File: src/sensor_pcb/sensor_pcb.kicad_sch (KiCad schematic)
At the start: 11 parts, among them Q1 NPN BJT 40V 200mA, U1 SHT45-AD1B, U2 16-bit ADC

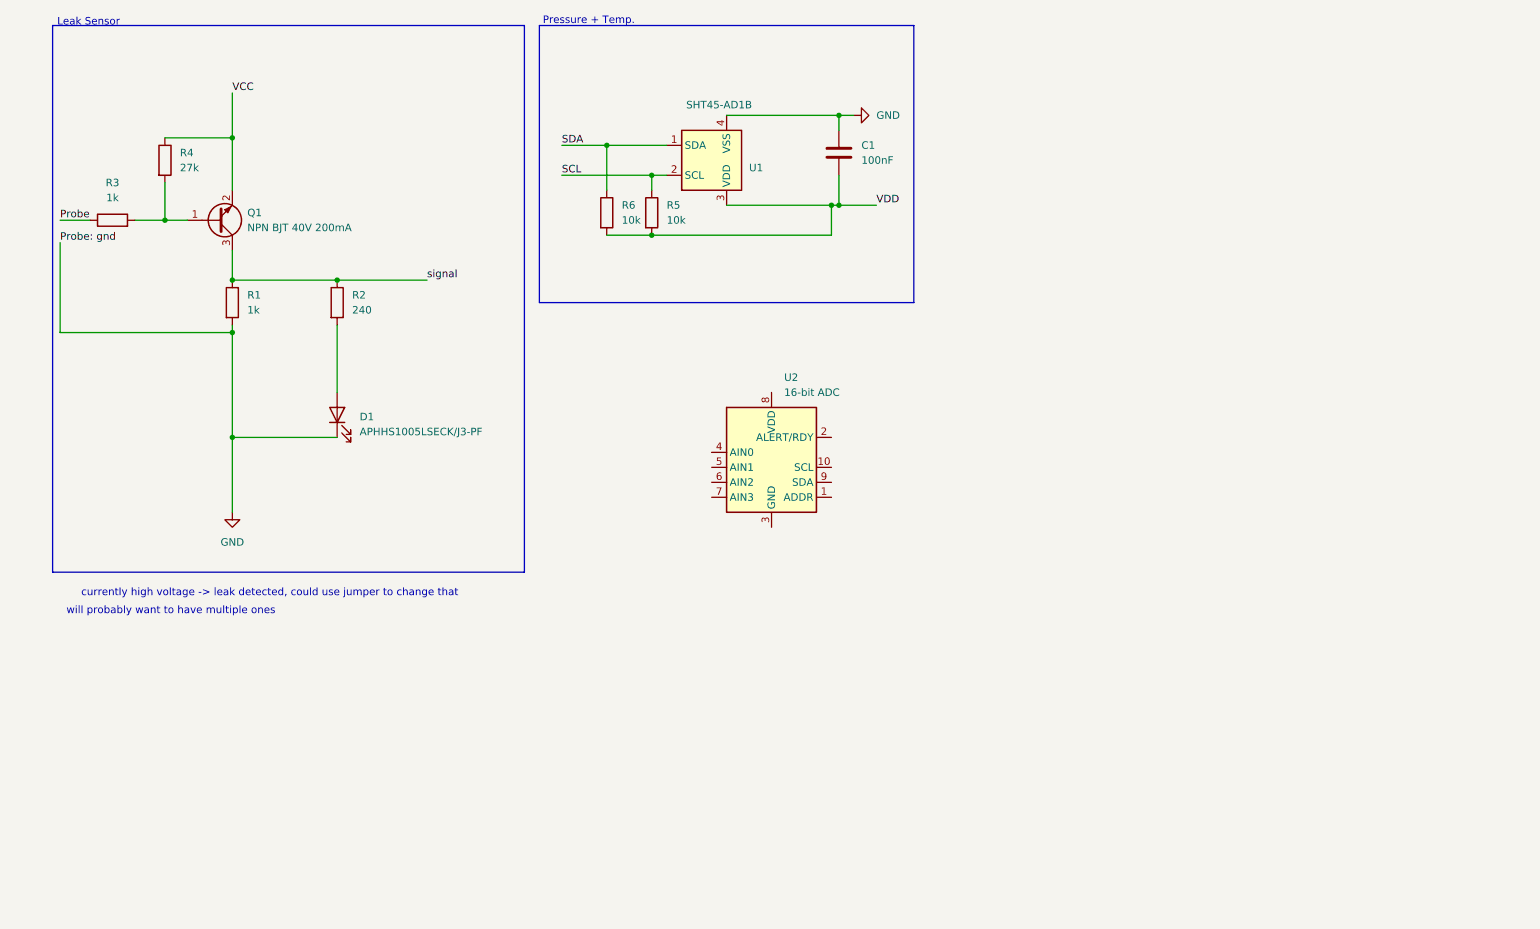
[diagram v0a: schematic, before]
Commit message: pressure sensor added
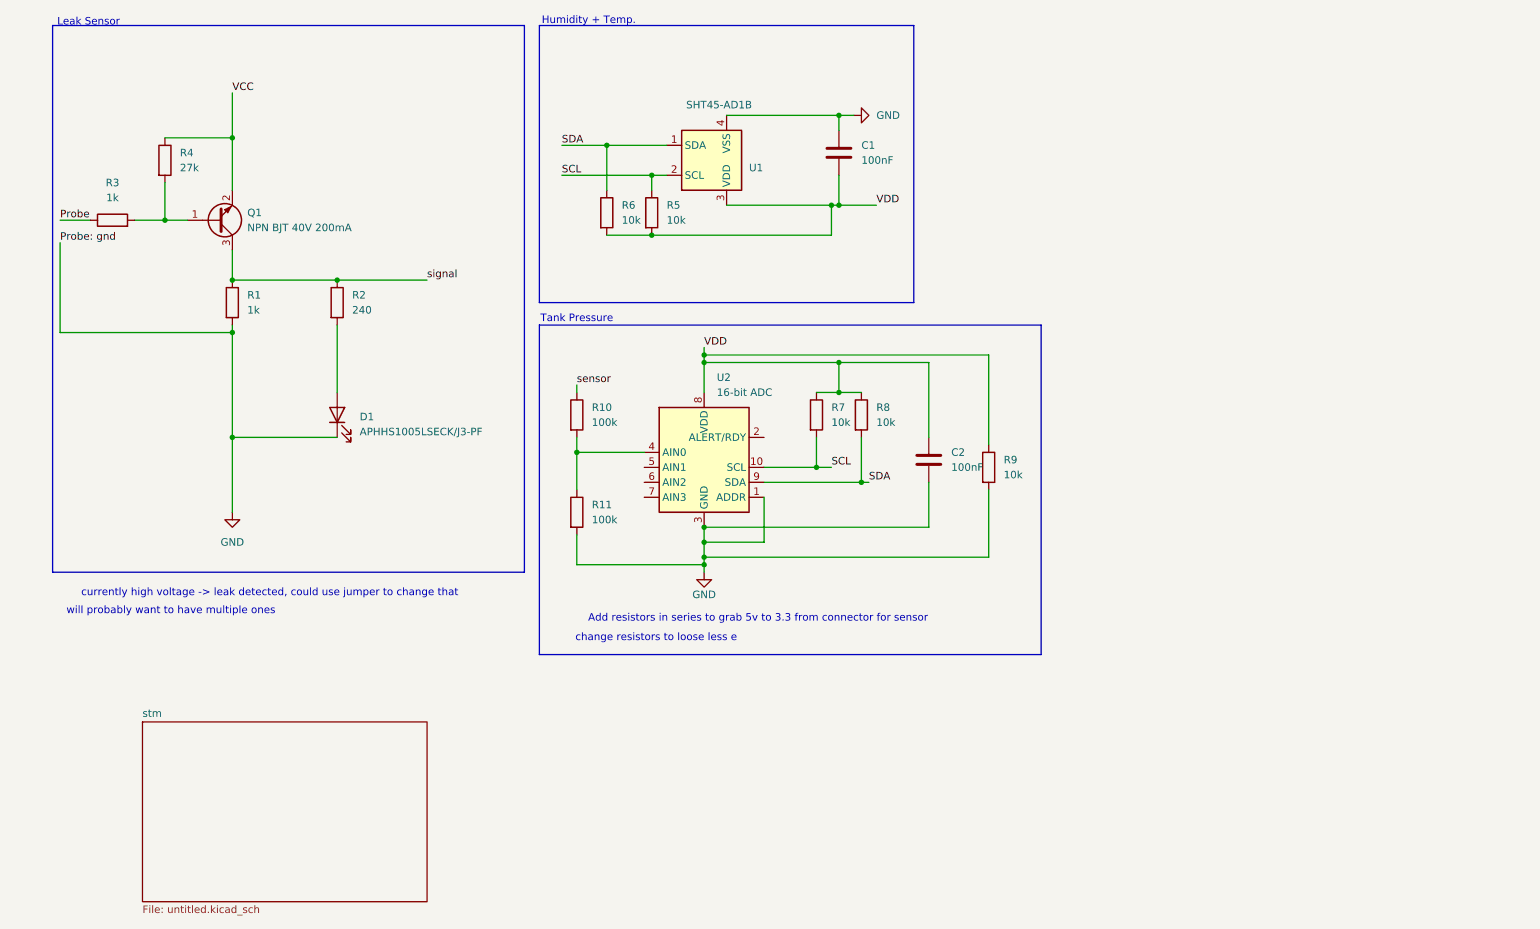
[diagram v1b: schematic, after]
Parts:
- added C2: 100nF, Capacitor_SMD:C_0402_1005Metric, symbol #dzdb:g_cap/C-100n-0402
- added R10, R11: 100k, Resistor_SMD:R_0603_1608Metric, symbol #dzdb:g_res/R-100k-0603
- added R7, R8, R9: 10k, Resistor_SMD:R_0603_1608Metric, symbol #dzdb:g_res/R-10k-0603
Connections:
- net GND: now also U2.1 (ADDR), U2.3 (GND), C2.2, R11.2, R9.2
- net SCL: now also U2.10 (SCL), R7.2
- net SDA: now also U2.9 (SDA), R8.2
- net VDD: now also U2.8 (VDD), C2.1, R7.1, R8.1, R9.1
- net at U2.4 (AIN0): now also R10.2, R11.1
- new net sensor: R10.1
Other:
- added sheet stm (untitled.kicad_sch)
- note added: "Add resistors in series to grab 5v to 3.3 from connector for sensor"
- note added: "Humidity + Temp."
- note added: "Tank Pressure"
- note added: "change resistors to loose less e"
- note removed: "Pressure + Temp."
- moved on the sheet: U2

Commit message: small fixes
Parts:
- removed R9: 10k, Resistor_SMD:R_0603_1608Metric, symbol #dzdb:g_res/R-10k-0603
- added C3, C4: 100nF, Capacitor_SMD:C_0201_0603Metric, symbol #dzdb:g_cap/C-100n-0201
- added U4: BMP581, dz_sens:BMP581, symbol #dzdb:s_sens/D-BOSCH-BMP581
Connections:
- net GND: now also C3.2, C4.2, U4.3 (VSS_1), U4.5 (SDO), U4.8 (VSS_2), U4.9 (VSS_3)
- net SCL: now also U4.2 (SCK)
- net SDA: now also U4.4 (SDI)
- net VDD: now also C3.1, C4.1, U4.1 (VDDIO), U4.10 (VDD), U4.6 (CSB)
- net sensor renamed p. sensor
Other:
- added sheet Leak_sensors (leak_sensors.kicad_sch)
- note added: "ADC for External Pressure"
- note added: "CAN Device"
- note added: "Can attach SDO to VDD instead to have 0x77 address instead of 0x76"
- note added: "Combine 10k resistors? Make them smaller?"
- note added: "Humidity + Temp. (Internal)"
- note added: "If we want to have interrupts we can tie INT to free input prin on MCU"
- note added: "Notes 100 nF decoupling could be centralized"
- note added: "Optimize resistors for voltage drop (5-3.3)"
- note added: "Part needs to be DGS package"
- note added: "Pressure Sensor (Internal)"
- note added: "Pressure Sensor (external)"
- note added: "Temperature Sensor (external)"
- note added: "Tie alert/rdy to GPIO for alerts"
- note removed: "Add resistors in series to grab 5v to 3.3 from connector for sensor"
- note removed: "Humidity + Temp."
- note removed: "Leak Sensor"
- note removed: "Tank Pressure"
- note removed: "change resistors to loose less e"
- moved on the sheet: C1, C2, R10, R11, R5, R6, R7, R8, U1, U2
